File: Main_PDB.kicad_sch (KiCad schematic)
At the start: 128 parts, among them J1 Conn_01x02_MountingPin, J10 Conn_01x02_MountingPin, J11 Conn_01x03_MountingPin, J12 Conn_01x02_MountingPin, J2 Conn_01x02_MountingPin, J3 Conn_01x02_MountingPin, J4 Conn_01x02_MountingPin, J5 Conn_01x02_MountingPin, J6 Conn_01x01_MountingPin, J7 Conn_01x01_MountingPin, J8 Conn_01x07_MountingPin, J9 Conn_01x03_MountingPin, Q1 PMOS, Q10 NMOS, Q14 NMOS, Q15 NMOS, Q2 NPN, Q7 NMOS, Q8 NMOS, Q9 NMOS, U1 LRM36015, U10 LM5148RGYR, U11 ACS758LCB-100U-PFF-T, U12 TPS48110AQDGXRQ1, U13 LM5148RGYR, U14 UCC27511DBVR, U2 ACS758LCB-100U-PFF-T, U4 ACS758LCB-100U-PFF-T, U5 ACS758LCB-100U-PFF-T, U6 ACS758LCB-100U-PFF-T, U8 ACS758LCB-100U-PFF-T, U9 ACS758LCB-100U-PFF-T

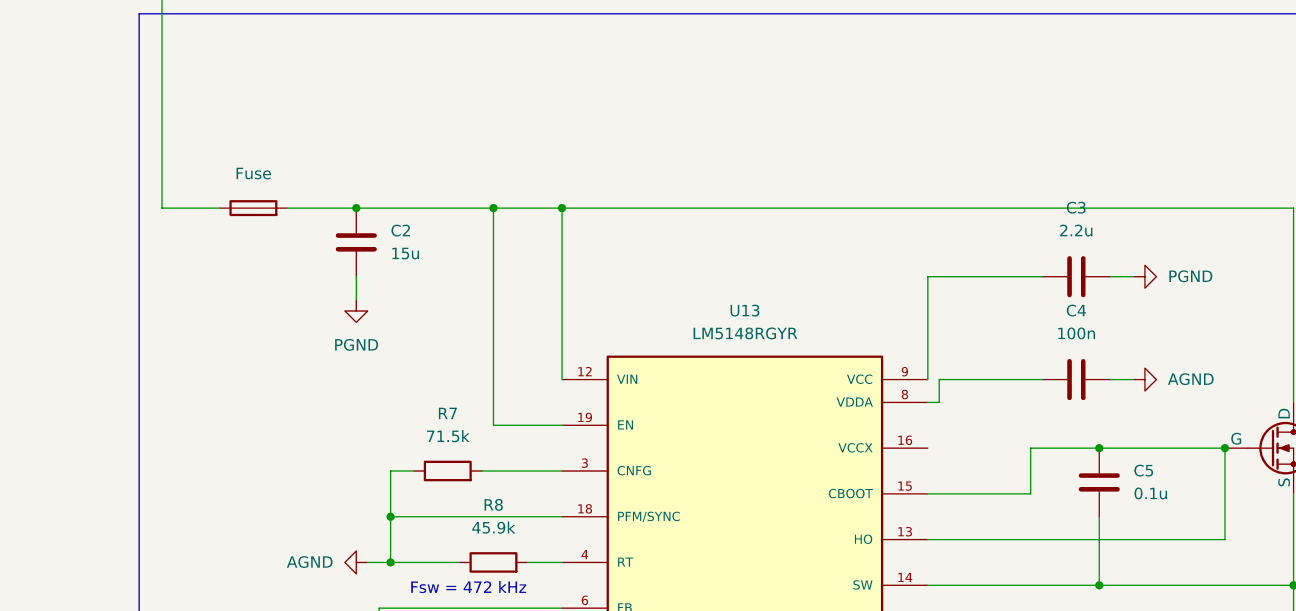
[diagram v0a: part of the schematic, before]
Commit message: Added input caps to 6V buck
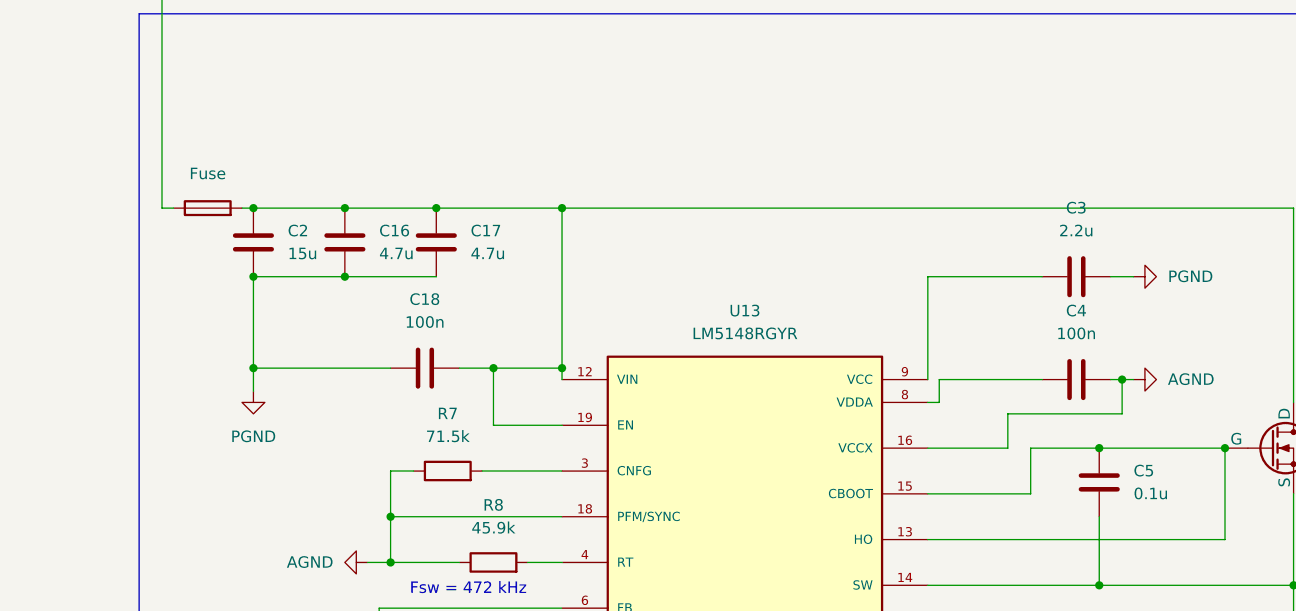
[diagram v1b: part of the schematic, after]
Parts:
- added C16, C17: 4.7u, symbol Device:C
- added C18: 100n, symbol Device:C
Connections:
- net AGND: now also U13.16 (VCCX)
- net PGND: now also C16.1, C17.1, C18.2
- net at C2.2, F7.2, Q14.1 (D)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: now also C16.2, C17.2, C18.1

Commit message: Thermistors edit
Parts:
- added R14, R15, R4: 10k, symbol Device:R
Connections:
- net +3.3V: now also R14.1, R15.1, R4.1; no longer TH1.2, TH2.2, TH3.2
- net AGND: now also TH1.2, TH2.2, TH3.2
- net at J11.1 (Pin_1), TH1.1: now also R4.2
- net at J11.3 (Pin_3), TH3.1: now also R15.2
- net at J11.2 (Pin_2), TH2.1: now also R14.2
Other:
- moved on the sheet: J11, TH1, TH2, TH3

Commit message: misc
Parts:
- removed C26, C27: 500u, symbol Device:C_Polarized
- added C32: 470u, symbol Device:C_Polarized
- added C51: 47u, symbol Device:C
- C28, C29, C30, C31: value 500u -> 470u
- C38: value 50u -> 470u
- L5: value 7.69u (30%) -> 7.5u (~30%)
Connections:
- net PGND: now also C32.2, C51.2
- net at C1.1, C28.1, C29.1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: now also C38.1, C32.1
- net at C39.1, C40.1, C49.1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: now also C51.1; no longer C38.1

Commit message: TVS diode grounding changes
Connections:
- net GND is gone; now on net PGND: D7.2 (A), D8.2 (A)
- net AGND: no longer U1.1 (PGND), U1.11 (PGND)
- net PGND: now also U1.1 (PGND), U1.11 (PGND)

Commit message: input/output caps on 3.3V rail update
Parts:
- removed CBOOT1: 100nF, symbol Device:C
- removed U1: LRM36015, symbol Amplifier_Current:INA199xxDCK
- added CBOOT2, CHF3, COUT3: 100nF, symbol Device:C
- added CIN2: 47uF, symbol Device:C
- added RENB2: 100R, symbol Device:R_US
- added U3: LMR36015ARNXR, RNX0012B, symbol LRM36015:LMR36015ARNXR
- J12: value Conn_01x02_MountingPin -> 3.3V output
- L1: value 27u (32.5%) or 33u (26.6%) -> 27uH (32.5%) or 33uH (26.6%)
- RENB1: renamed from RFBB1; value 43.2KR -> 43k
- RENT1: renamed from RFBT1; value 100KR -> 100k
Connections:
- net PGND is gone; now on net +48V-B: C10.2, C11.2, C12.2, C13.2, C14.2, C15.2, C16.1, C17.1, C18.2, C19.2, C2.1, C20.2, C21.2, C22.2, C23.2, C24.2, C28.2, C29.2, C3.2, C30.2, C31.2, C32.2, C38.2, C39.2, C40.2, C41.2, C43.2, C44.2, C46.2, C48.2, C49.2, C51.2, C6.2, C7.2, C8.2, C9.2, CHF1.2, CHF2.2, CIN1.2, D1.2 (A), D2.2 (A), D3.2 (A), D4.2 (A), D5.2 (A), D6.2 (A), D7.2 (A), D8.2 (A), J1.2 (Pin_2), J10.2 (Pin_2), J2.2 (Pin_2), J3.2 (Pin_2), J4.2 (Pin_2), J5.2 (Pin_2), Q15.3 (S), Q2.3 (E), Q9.3 (S), R1.2, R12.2, R21.2, U10.10 (PGND), U10.25 (EP), U13.10 (PGND), U13.25 (EP)
- net +3.3V: now also COUT3.1
- net +48V-B: now also C33.2, C34.2, C35.2, C36.2, C37.2, C4.2, C45.2, C47.2, C50.1, C53.2, COUT1.2, COUT2.2, CVCC1.1, J12.2 (Pin_2), R17.1, R18.1, R7.1, R8.1, TH1.2, TH2.2, TH3.2, U10.16 (VCCX), U10.18 (PFM/SYNC), U10.7 (AGND), U11.2 (GND), U12.10 (DIODE), U12.2 (OV), U12.6 (GND), U12.7 (IMON), U12.8 (IWRN), U12.9 (TMR), U13.16 (VCCX), U13.18 (PFM/SYNC), U13.7 (AGND), U14.4 (GND), U14.5 (IN-), U2.2 (GND), U4.2 (GND), U5.2 (GND), U6.2 (GND), U8.2 (GND), U9.2 (GND), CHF3.2, CIN2.1, COUT3.2, RENB2.1, U3.1 (PGND), U3.11 (PGND), U3.6 (AGND)
- net at CFF1.2, RENB1.2, RENT1.1: now also U3.7 (FB)
- net at CHF1.1, CHF2.1, CIN1.1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: now also CHF3.1, CIN2.2, U3.10 (VIN), U3.2 (VIN), U3.9 (EN)
- net at CVCC1.2: now also U3.5 (VCC)
- net at L1.1: now also CBOOT2.2, U3.12 (SW), U3.3 (NC)
- removed net AGND: C33.2, C34.2, C35.2, C36.2, C37.2, C4.2, C45.2, C47.2, C50.1, C53.2, COUT1.2, COUT2.2, CVCC1.1, J12.2 (Pin_2), R17.1, R18.1, R7.1, R8.1, RENB1.1, TH1.2, TH2.2, TH3.2, U10.16 (VCCX), U10.18 (PFM/SYNC), U10.7 (AGND), U11.2 (GND), U12.10 (DIODE), U12.2 (OV), U12.6 (GND), U12.7 (IMON), U12.8 (IWRN), U12.9 (TMR), U13.16 (VCCX), U13.18 (PFM/SYNC), U13.7 (AGND), U14.4 (GND), U14.5 (IN-), U2.2 (GND), U4.2 (GND), U5.2 (GND), U6.2 (GND), U8.2 (GND), U9.2 (GND)
- new net: RENB1.1, RENB2.2
- new net: CBOOT2.1, U3.4 (BST)
- no-connect marks 15 -> 16
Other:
- note added: "400KHZ SF"
- note removed: "400KHZ FS"
- moved on the sheet: CFF1, CHF1, CHF2, CIN1, COUT1, COUT2, CVCC1, J12, L1, RENB1, RENT1

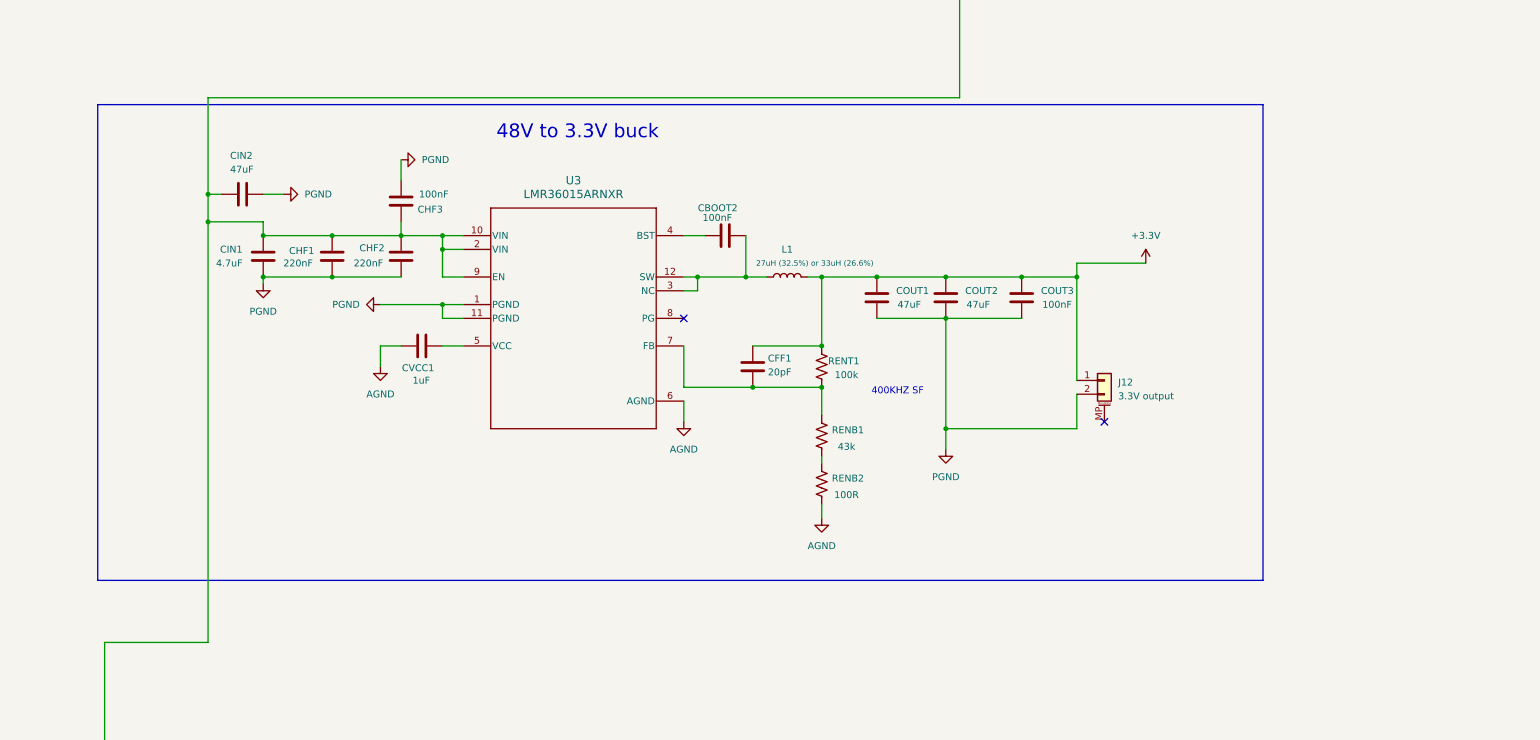
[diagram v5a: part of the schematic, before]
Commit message: Revisions for 3.3V buck + Added footprints
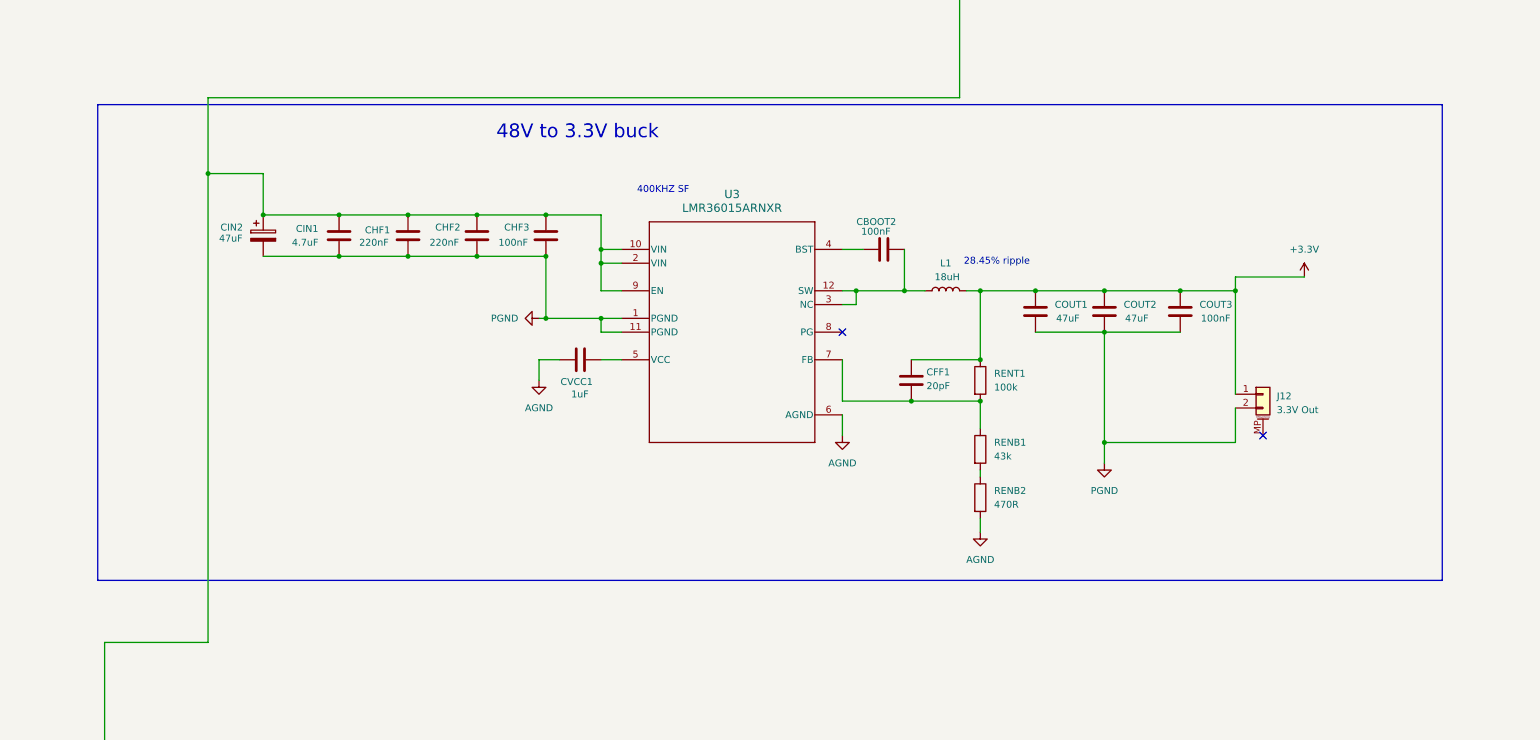
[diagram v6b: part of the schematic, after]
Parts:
- removed CIN2: 47uF, symbol Device:C
- removed RENB1: 43k, symbol Device:R_US
- removed RENB2: 100R, symbol Device:R_US
- removed RENT1: 100k, symbol Device:R_US
- added CIN2: 47uF, Capacitor_SMD:CP_Elec_10x10.5, symbol Device:C_Polarized
- added RENB1: 43k, Resistor_SMD:R_0603_1608Metric, symbol Device:R
- added RENB2: 470R, Resistor_SMD:R_0603_1608Metric, symbol Device:R
- added RENT1: 100k, Resistor_SMD:R_0603_1608Metric, symbol Device:R
- CBOOT2, CFF1, COUT3: footprint (none) -> Capacitor_SMD:C_0603_1608Metric; Voltage (none) -> 16V
- CHF1, CHF2, CHF3: footprint (none) -> Capacitor_SMD:C_0805_2012Metric; Voltage (none) -> 100V
- CIN1: footprint (none) -> Capacitor_SMD:C_1210_3225Metric; Voltage (none) -> 100V
- COUT1, COUT2: footprint (none) -> Capacitor_SMD:C_1210_3225Metric; Voltage (none) -> 16V
- CVCC1: footprint (none) -> Capacitor_SMD:C_0805_2012Metric; Voltage (none) -> 16V
- J12: value 3.3V output -> 3.3V Out
- L1: value 27uH (32.5%) or 33uH (26.6%) -> 18uH; footprint (none) -> Footprints:MSS1038183MLC
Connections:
- net +3.3V: now also RENT1.1
- net +48V-B: now also CIN2.2, RENB2.2
- net at CFF1.2, U3.7 (FB): now also RENB1.1, RENT1.2
- net at CHF1.1, CHF2.1, CHF3.1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: now also CIN2.1
- new net: RENB1.2, RENB2.1
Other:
- note added: "28.45% ripple"
- moved on the sheet: CBOOT2, CFF1, CHF1, CHF2, CHF3, CIN1, COUT1, COUT2, COUT3, CVCC1, J12, L1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

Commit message: Started updating 48->12 buck footprints (caps and res)
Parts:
- removed C15: 220u, symbol Device:C_Polarized
- removed C40: 4.7u, symbol Device:C
- removed C46, C48: 22u, symbol Device:C
- removed C49: 100n, symbol Device:C
- removed C51: 47u, symbol Device:C
- added CBULK1: 220uF, Capacitor_SMD:CP_Elec_10x10.5, symbol Device:C_Polarized
- added CIN1B: 47uF, Capacitor_SMD:CP_Elec_10x10.5, symbol Device:C_Polarized
- added CIN2B1: 4.7u, Capacitor_SMD:C_1210_3225Metric, symbol Device:C
- added CIN4B, COUT4B: 100nF, Capacitor_SMD:C_0805_2012Metric, symbol Device:C
- added COUT1B, COUT2B, COUT3B: 22uF, Capacitor_SMD:C_1210_3225Metric, symbol Device:C
- CBOOT2: renamed from C42; footprint (none) -> Capacitor_SMD:C_0603_1608Metric; Voltage (none) -> 16V
- CCOMP: renamed from C44; value 820p -> 6.8nF; footprint (none) -> Capacitor_SMD:C_0603_1608Metric; Voltage (none) -> 16V
- CCS1: renamed from C47; footprint (none) -> Capacitor_SMD:C_0603_1608Metric; Voltage (none) -> 16V
- CHF: renamed from C43; value 30p -> 100pF; footprint (none) -> Capacitor_SMD:C_0603_1608Metric
- CIN2B: renamed from C39; footprint (none) -> Capacitor_SMD:C_1210_3225Metric; Voltage (none) -> 100V
- CVCC2: renamed from C41; footprint (none) -> Capacitor_SMD:C_0805_2012Metric; Voltage (none) -> 16V
- CVDDA2: renamed from C45; footprint (none) -> Capacitor_SMD:C_0805_2012Metric; Voltage (none) -> 16V
- R17, R18, R20, R21: footprint (none) -> Resistor_SMD:R_0603_1608Metric
- RCOMP: renamed from R19; value 4.64k -> 4.75k; footprint (none) -> Resistor_SMD:R_0603_1608Metric
- U3: footprint RNX0012B -> Footprints:RNX0012B
- renumbered CBOOT2 to CBOOT1, CHF2 to CHF4A, CIN2 to CIN1A, CIN1 to CIN2A, CHF1 to CIN3A, CHF3 to CIN5A, COUT1 to COUT1A, COUT2 to COUT2A, COUT3 to COUT3A, CVCC1 to CVCCA
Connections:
- net +48V-B: no longer C10.2, C11.2, C12.2, C13.2, C14.2, C16.1, C17.1, C18.2, C19.2, C2.1, C20.2, C21.2, C22.2, C23.2, C24.2, C28.2, C29.2, C3.2, C30.2, C31.2, C32.2, C33.1, C33.2, C34.2, C35.2, C36.2, C37.2, C38.2, C4.2, C50.1, C53.2, C6.2, C7.2, C8.2, C9.2, CCOMP.2, CCS1.2, CHF.2, CHF4A.2, CIN1A.2, CIN2A.2, CIN2B.2, CIN3A.2, CIN5A.2, COUT1A.2, COUT2A.2, COUT3A.2, CVCC2.2, CVCCA.1, CVDDA2.2, D1.2 (A), D2.2 (A), D3.2 (A), D4.2 (A), D5.2 (A), D6.2 (A), D7.2 (A), D8.2 (A), J1.2 (Pin_2), J10.2 (Pin_2), J12.2 (Pin_2), J2.2 (Pin_2), J3.2 (Pin_2), J4.2 (Pin_2), J5.2 (Pin_2), Q15.3 (S), Q2.3 (E), Q9.3 (S), R1.2, R12.2, R17.1, R18.1, R21.2, R7.1, R8.1, RENB2.2, TH1.2, TH2.2, TH3.2, U10.10 (PGND), U10.16 (VCCX), U10.18 (PFM/SYNC), U10.25 (EP), U10.7 (AGND), U11.2 (GND), U12.10 (DIODE), U12.2 (OV), U12.6 (GND), U12.7 (IMON), U12.8 (IWRN), U12.9 (TMR), U13.10 (PGND), U13.16 (VCCX), U13.18 (PFM/SYNC), U13.25 (EP), U13.7 (AGND), U14.4 (GND), U14.5 (IN-), U2.2 (GND), U3.1 (PGND), U3.11 (PGND), U3.6 (AGND), U4.2 (GND), U5.2 (GND), U6.2 (GND), U8.2 (GND), U9.1 (VCC), U9.2 (GND)
- net at R20.1, R22.2, U10.21 (VOUT)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: now also COUT1B.1, COUT2B.1, COUT3B.1, COUT4B.1
- net at F6.2, Q8.1 (D), U10.12 (VIN)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: now also CIN2B.2, CIN1B.1, CIN2B1.2, CIN4B.2; no longer CIN2B.1
- net at D8.1 (K), J1.1 (Pin_1), U11.5 (IP-)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: now also CBULK1.1
- new net +5V: C33.1, U9.1 (VCC)
- new net AGND: C10.2, C11.2, C12.2, C13.2, C14.2, C16.1, C17.1, C18.2, C19.2, C2.1, C20.2, C21.2, C22.2, C23.2, C24.2, C28.2, C29.2, C3.2, C30.2, C31.2, C32.2, C33.2, C34.2, C35.2, C36.2, C37.2, C38.2, C4.2, C50.1, C53.2, C6.2, C7.2, C8.2, C9.2, CBULK1.2, CCOMP.2, CCS1.2, CHF.2, CHF4A.2, CIN1A.2, CIN1B.2, CIN2A.2, CIN2B.1, CIN2B1.1, CIN3A.2, CIN4B.1, CIN5A.2, COUT1A.2, COUT1B.2, COUT2A.2, COUT2B.2, COUT3A.2, COUT3B.2, COUT4B.2, CVCC2.2, CVCCA.1, CVDDA2.2, D1.2 (A), D2.2 (A), D3.2 (A), D4.2 (A), D5.2 (A), D6.2 (A), D7.2 (A), D8.2 (A), J1.2 (Pin_2), J10.2 (Pin_2), J12.2 (Pin_2), J2.2 (Pin_2), J3.2 (Pin_2), J4.2 (Pin_2), J5.2 (Pin_2), Q15.3 (S), Q2.3 (E), Q9.3 (S), R1.2, R12.2, R17.1, R18.1, R21.2, R7.1, R8.1, RENB2.2, TH1.2, TH2.2, TH3.2, U10.10 (PGND), U10.16 (VCCX), U10.18 (PFM/SYNC), U10.25 (EP), U10.7 (AGND), U11.2 (GND), U12.10 (DIODE), U12.2 (OV), U12.6 (GND), U12.7 (IMON), U12.8 (IWRN), U12.9 (TMR), U13.10 (PGND), U13.16 (VCCX), U13.18 (PFM/SYNC), U13.25 (EP), U13.7 (AGND), U14.4 (GND), U14.5 (IN-), U2.2 (GND), U3.1 (PGND), U3.11 (PGND), U3.6 (AGND), U4.2 (GND), U5.2 (GND), U6.2 (GND), U8.2 (GND), U9.2 (GND)
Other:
- moved on the sheet: CCOMP, CCS1, CHF, CIN2B, D8, J1, RCOMP, U11

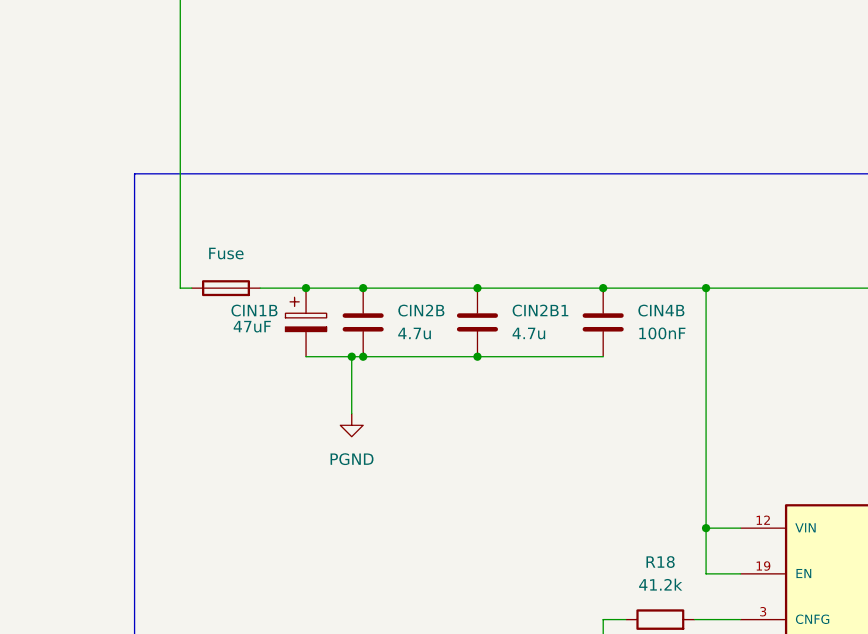
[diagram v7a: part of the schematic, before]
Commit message: Added input cap to 48->12 buck
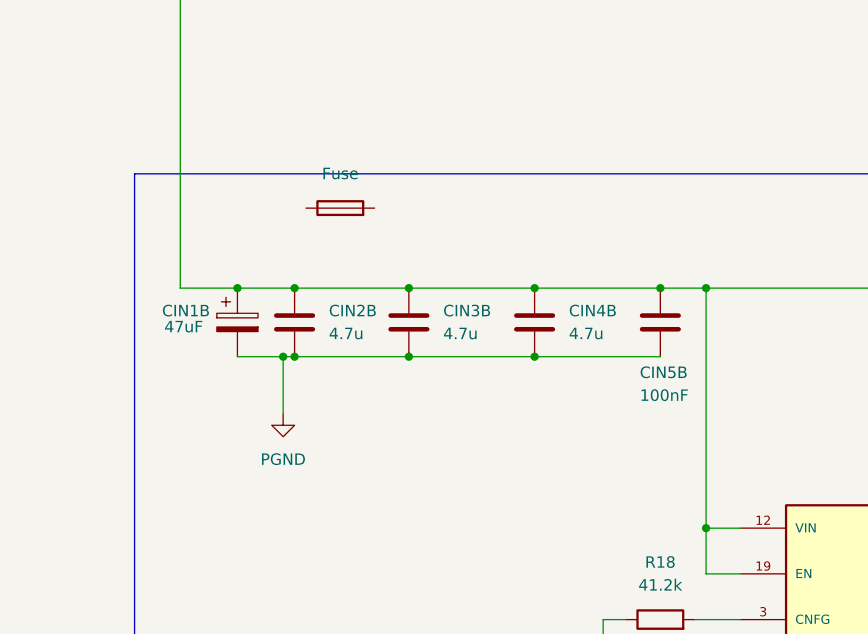
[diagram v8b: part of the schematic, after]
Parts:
- removed F6: Fuse, symbol Device:Fuse
- added CIN4B: 4.7u, Capacitor_SMD:C_1210_3225Metric, symbol Device:C
- added F8: Fuse, symbol Device:Fuse
- renumbered CIN2B1 to CIN3B, CIN4B to CIN5B
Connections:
- net AGND: now also CIN4B.1
- net at CIN1B.1, CIN2B.2, CIN3B.2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: now also CHF4A.1, CIN1A.1, CIN2A.1, CIN3A.1, CIN5A.1, J7.1 (Pin_1), U3.10 (VIN), U3.2 (VIN), U3.9 (EN), U9.5 (IP-), U9.5_1 (IP-), U9.5_10 (IP-), U9.5_11 (IP-), U9.5_12 (IP-), U9.5_13 (IP-), U9.5_14 (IP-), U9.5_15 (IP-), U9.5_16 (IP-), U9.5_2 (IP-), U9.5_3 (IP-), U9.5_4 (IP-), U9.5_5 (IP-), U9.5_6 (IP-), U9.5_7 (IP-), U9.5_8 (IP-), U9.5_9 (IP-), CIN4B.2
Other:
- moved on the sheet: CIN1B, CIN2B, CIN3B, CIN5B
